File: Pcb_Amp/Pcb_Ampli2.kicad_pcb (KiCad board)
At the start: 4 copper layers, 83.1 x 55.7 mm, 56 parts, among them J1 Conn_01x02, J2 Jack-DC, J3 Jack-DC, J4 Conn_01x02, SW1 SW_SPDT

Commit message: PCBV3_Preamp_Power
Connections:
- R5 pad 1: Net-(R5-Pad1) -> GND
- R6 pad 2: Net-(R5-Pad1) -> GND
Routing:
- net GND: track 42.2 -> 46.3 mm, vias 14 -> 15
- net Net-(R5-Pad1): track 3.92 -> 0.00 mm
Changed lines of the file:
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@@
 	(net 32 "Net-(C34-Pad1)")
 	(net 33 "Net-(J1-Pin_2)")
-	(net 34 "Net-(R5-Pad1)")
-	(net 35 "Net-(TPA1-7_OC_ADJ)")
-	(net 36 "Net-(TPA1-8_FREQ_ADJ)")
-	(net 37 "Net-(R10-Pad1)")
-	(net 38 "unconnected-(SW1-C-Pad3)")
+	(net 34 "Net-(TPA1-7_OC_ADJ)")
+	(net 35 "Net-(TPA1-8_FREQ_ADJ)")
+	(net 36 "Net-(R10-Pad1)")
+	(net 37 "unconnected-(SW1-C-Pad3)")
 	(footprint "Capacitor_SMD:C_0805_2012Metric"
 		(layer "F.Cu")
@@
 			(layers "F.Cu" "F.Mask" "F.Paste")
 			(roundrect_rratio 0.25)
-			(net 34 "Net-(R5-Pad1)")
+			(net 1 "GND")
 			(pintype "passive")
 		)
@@
 			(layers "F.Cu" "F.Mask" "F.Paste")
 			(roundrect_rratio 0.243902)
-			(net 35 "Net-(TPA1-7_OC_ADJ)")
+			(net 34 "Net-(TPA1-7_OC_ADJ)")
 			(pintype "passive")
 		)
@@
 			(layers "F.Cu" "F.Mask" "F.Paste")
 			(roundrect_rratio 0.25)
-			(net 37 "Net-(R10-Pad1)")
+			(net 36 "Net-(R10-Pad1)")
 			(pintype "passive")
 		)
@@
 			(layers "F.Cu" "F.Mask" "F.Paste")
 			(roundrect_rratio 0.25)
-			(net 34 "Net-(R5-Pad1)")
+			(net 1 "GND")
 			(pintype "passive")
 		)
@@
 			(layers "F.Cu" "F.Mask" "F.Paste")
 			(roundrect_rratio 0.25)
-			(net 37 "Net-(R10-Pad1)")
+			(net 36 "Net-(R10-Pad1)")
 			(pintype "passive")
 		)
@@
 			(size 0.399999 1.4)
 			(layers "F.Cu" "F.Mask" "F.Paste")
-			(net 35 "Net-(TPA1-7_OC_ADJ)")
+			(net 34 "Net-(TPA1-7_OC_ADJ)")
 		)
 		(pad "8_FREQ_ADJ" smd oval
@@
 			(size 0.399999 1.4)
 			(layers "F.Cu" "F.Mask" "F.Paste")
-			(net 36 "Net-(TPA1-8_FREQ_ADJ)")
+			(net 35 "Net-(TPA1-8_FREQ_ADJ)")
 		)
 		(pad "9_OSC_IOM" smd oval
@@
 			(layers "*.Cu" "*.Mask")
 			(remove_unused_layers no)
-			(net 38 "unconnected-(SW1-C-Pad3)")
+			(net 37 "unconnected-(SW1-C-Pad3)")
 			(pinfunction "C")
 			(pintype "passive+no_connect")
@@
 			(layers "F.Cu" "F.Mask" "F.Paste")
 			(roundrect_rratio 0.25)
-			(net 36 "Net-(TPA1-8_FREQ_ADJ)")
+			(net 35 "Net-(TPA1-8_FREQ_ADJ)")
 			(pintype "passive")
 		)
@@
 	)
 	(segment
+		(start 128.425 61.3)
+		(end 128.425 62.825)
+		(width 0.16)
+		(layer "F.Cu")
+		(net 1)
+	)
+	(segment
+		(start 128.325 62.85)
+		(end 128.45 62.85)
+		(width 0.16)
+		(layer "F.Cu")
+		(net 1)
+	)
+	(segment
 		(start 121.25 86.85)
 		(end 121.3 86.9)
@@
 	)
 	(segment
+		(start 126.675 64.5)
+		(end 128.325 62.85)
+		(width 0.16)
+		(layer "F.Cu")
+		(net 1)
+	)
+	(segment
 		(start 99.4975 67.9025)
 		(end 99.7 67.7)
@@
 	)
 	(segment
+		(start 128.425 62.825)
+		(end 128.45 62.85)
+		(width 0.16)
+		(layer "F.Cu")
+		(net 1)
+	)
+	(segment
 		(start 93.3 72.275)
 		(end 93.325 72.3)
@@
 	)
 	(via
+		(at 128.45 62.85)
+		(size 0.45)
+		(drill 0.3)
+		(layers "F.Cu" "B.Cu")
+		(net 1)
+	)
+	(via
 		(at 107.65 73.35)
 		(size 0.45)
@@
 	)
 	(segment
-		(start 126.675 63.05)
-		(end 128.425 61.3)
-		(width 0.16)
-		(layer "F.Cu")
-		(net 34)
-	)
-	(segment
-		(start 126.675 64.5)
-		(end 126.675 63.05)
-		(width 0.16)
-		(layer "F.Cu")
-		(net 34)
-	)
-	(segment
 		(start 90.7 68.9)
 		(end 91.4 69.6)
 		(width 0.25)
 		(layer "F.Cu")
-		(net 35)
+		(net 34)
 	)
 	(segment
@@
 		(width 0.16)
 		(layer "F.Cu")
-		(net 35)
+		(net 34)
 	)
 	(segment
@@
 		(width 0.25)
 		(layer "F.Cu")
-		(net 35)
+		(net 34)
 	)
 	(segment
@@
 		(width 0.25)
 		(layer "F.Cu")
-		(net 35)
+		(net 34)
 	)
 	(segment
@@
 		(width 0.16)
 		(layer "F.Cu")
-		(net 35)
+		(net 34)
 	)
 	(via
@@
 		(drill 0.3)
 		(layers "F.Cu" "B.Cu")
-		(net 35)
+		(net 34)
 	)
 	(via
@@
 		(drill 0.3)
 		(layers "F.Cu" "B.Cu")
-		(net 35)
+		(net 34)
 	)
 	(segment
@@
 		(width 0.16)
 		(layer "B.Cu")
-		(net 35)
+		(net 34)
 	)
 	(segment
@@
 		(width 0.16)
 		(layer "B.Cu")
-		(net 35)
+		(net 34)
 	)
 	(segment
@@
 		(width 0.16)
 		(layer "F.Cu")
-		(net 36)
+		(net 35)
 	)
 	(segment
@@
 		(width 0.16)
 		(layer "F.Cu")
-		(net 36)
+		(net 35)
 	)
 	(segment
@@
 		(width 0.16)
 		(layer "F.Cu")
-		(net 36)
+		(net 35)
 	)
 	(segment
@@
 		(width 0.16)
 		(layer "F.Cu")
-		(net 36)
+		(net 35)
 	)
 	(via
@@
 		(drill 0.3)
 		(layers "F.Cu" "B.Cu")
-		(net 36)
+		(net 35)
 	)
 	(via
@@
 		(drill 0.3)
 		(layers "F.Cu" "B.Cu")
-		(net 36)
+		(net 35)
 	)
 	(segment
@@
 		(width 0.16)
 		(layer "B.Cu")
-		(net 36)
+		(net 35)
 	)
 	(segment
@@
 		(width 0.16)
 		(layer "B.Cu")
-		(net 36)
+		(net 35)
 	)
 	(segment
@@
 		(width 0.16)
 		(layer "B.Cu")
-		(net 36)
+		(net 35)
 	)
 	(segment
@@
 		(width 0.16)
 		(layer "F.Cu")
-		(net 37)
+		(net 36)
 	)
 	(segment
@@
 		(width 0.16)
 		(layer "F.Cu")
-		(net 37)
+		(net 36)
 	)
 	(zone

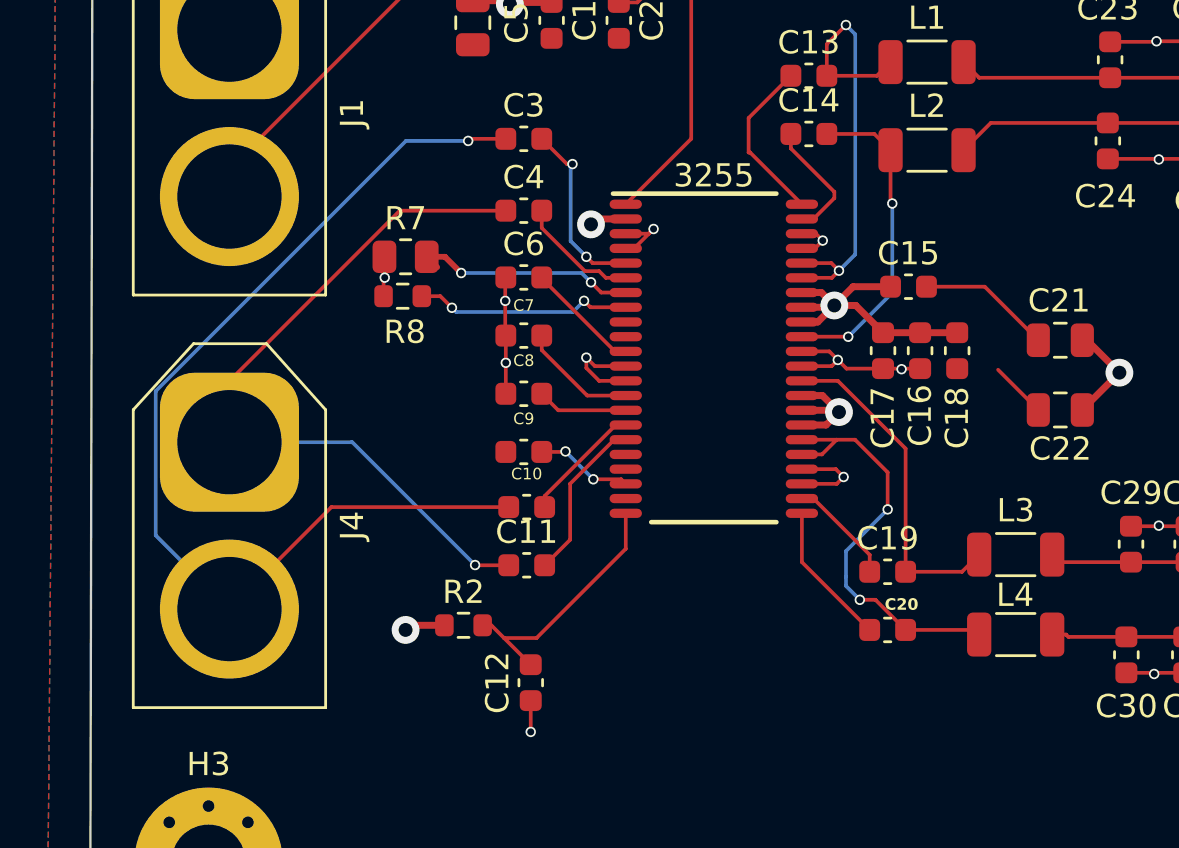
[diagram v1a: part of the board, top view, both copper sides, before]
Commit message: PCBV4_Connectors_changed
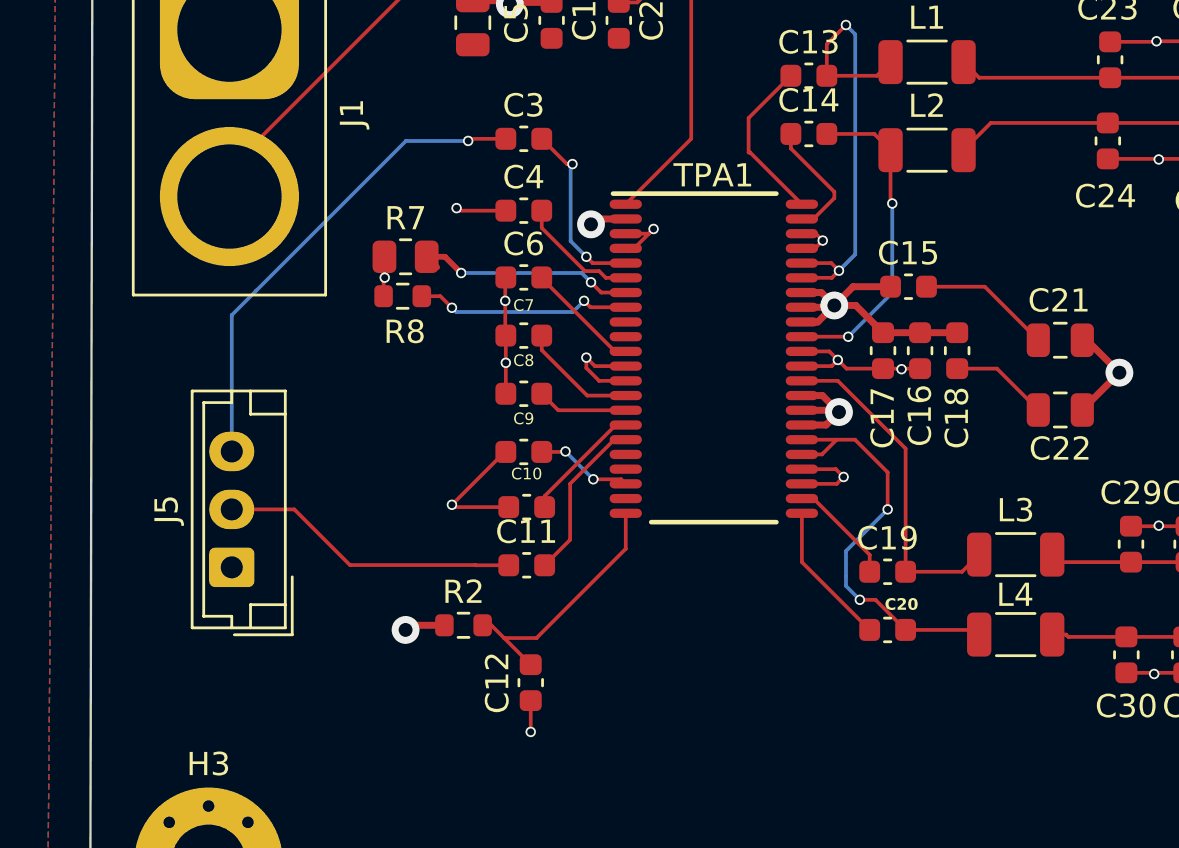
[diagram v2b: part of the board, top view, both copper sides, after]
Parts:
- removed J4: Conn_01x02, Connector_AMASS:AMASS_XT60-M_1x02_P7.20mm_Vertical
- added J5: Conn_01x03, Connector_JST:JST_EH_B3B-EH-A_1x03_P2.50mm_Vertical, F.Cu at (81.5, 82.3)
- renumbered 3255 to TPA1
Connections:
- C10 pad 1: Net-(J4-Pin_2) -> GND
- C11 pad 1: Net-(J4-Pin_1) -> Net-(J5-Pin_2)
- C3 pad 1: Net-(J4-Pin_2) -> Net-(J5-Pin_3)
- C4 pad 1: Net-(J4-Pin_1) -> GND
- R10 pad 1: Net-(R10-Pad1) -> GND
- R9 pad 2: Net-(R10-Pad1) -> GND
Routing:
- net Net-(J4-Pin_2): track 44.2 -> 0.00 mm, vias 1 -> 0
- net Net-(J4-Pin_1): track 31.9 -> 0.00 mm, vias 1 -> 0
- net Net-(J5-Pin_3): track 0.00 -> 20.9 mm, vias 0 -> 1
- net Net-(J5-Pin_2): track 0.00 -> 12.9 mm
- net GND: track 46.3 -> 57.2 mm, vias 15 -> 17
- net Net-(R10-Pad1): track 3.59 -> 0.00 mm
- net Net-(C18-Pad1): track 2.45 -> 4.24 mm
